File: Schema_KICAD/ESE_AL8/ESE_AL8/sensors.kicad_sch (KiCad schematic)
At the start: 22 parts, among them J201 JTAG/SWD, J202 LIDAR, J203 CB1, J204 CB3, J205 CB2, J206 CB4, J207 Moteur1, J208 Moteur2, SW201 SWITCH_CHANGEMENT, U201 ADXL343, U202 ZXBM5210-SP, U203 ZXBM5210-SP

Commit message: schema_architectural
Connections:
- net +3.3V: now also J207.5 (Pin_5), J208.5 (Pin_5)
- net +5V: no longer J207.5 (Pin_5), J208.5 (Pin_5)
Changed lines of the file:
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@@
 	)
 	(symbol
+		(lib_name "+3.3V_1")
+		(lib_id "power:+3.3V")
+		(at 115.57 167.64 90)
+		(unit 1)
+		(exclude_from_sim no)
+		(in_bom yes)
+		(on_board yes)
+		(dnp no)
+		(fields_autoplaced yes)
+		(property "Reference" "#PWR02"
+			(at 119.38 167.64 0)
+			(effects
+				(font
+					(size 1.27 1.27)
+				)
+				(hide yes)
+			)
+		)
+		(property "Value" "+3.3V"
+			(at 111.76 167.6399 90)
+			(effects
+				(font
+					(size 1.27 1.27)
+				)
+				(justify left)
+			)
+		)
+		(property "Footprint" ""
+			(at 115.57 167.64 0)
+			(effects
+				(font
+					(size 1.27 1.27)
+				)
+				(hide yes)
+			)
+		)
+		(property "Datasheet" ""
+			(at 115.57 167.64 0)
+			(effects
+				(font
+					(size 1.27 1.27)
+				)
+				(hide yes)
+			)
+		)
+		(property "Description" "Power symbol creates a global label with name \"+3.3V\""
+			(at 115.57 167.64 0)
+			(effects
+				(font
+					(size 1.27 1.27)
+				)
+				(hide yes)
+			)
+		)
+		(pin "1"
+		)
+		(instances
+			(project "ESE_AL8"
+				(path "/c3d0eb52-cd9d-4e69-bcf7-3f0716f715c6/ec07ab64-4612-44cf-8e70-ea693fb6c5ed"
+					(reference "#PWR02")
+					(unit 1)
+				)
+			)
+		)
+	)
+	(symbol
 		(lib_id "Device:C_Small")
 		(at 190.5 36.83 0)
@@
 	)
 	(symbol
-		(lib_id "power:+5V")
-		(at 115.57 167.64 90)
+		(lib_id "power:GND")
+		(at 46.99 62.23 0)
 		(unit 1)
 		(exclude_from_sim no)
@@
 		(dnp no)
 		(fields_autoplaced yes)
-		(property "Reference" "#PWR0234"
-			(at 119.38 167.64 0)
+		(property "Reference" "#PWR0211"
+			(at 46.99 68.58 0)
 			(effects
 				(font
@@
 			)
 		)
-		(property "Value" "+5V"
-			(at 111.76 167.64 90)
+		(property "Value" "GND"
+			(at 46.99 67.31 0)
 			(effects
 				(font
 					(size 1.27 1.27)
 				)
-				(justify left)
 			)
 		)
 		(property "Footprint" ""
-			(at 115.57 167.64 0)
+			(at 46.99 62.23 0)
 			(effects
 				(font
@@
 		)
 		(property "Datasheet" ""
-			(at 115.57 167.64 0)
+			(at 46.99 62.23 0)
 			(effects
 				(font
@@
 		)
 		(property "Description" ""
-			(at 115.57 167.64 0)
+			(at 46.99 62.23 0)
 			(effects
 				(font
@@
 			(project "ESE_AL8"
 				(path "/c3d0eb52-cd9d-4e69-bcf7-3f0716f715c6/ec07ab64-4612-44cf-8e70-ea693fb6c5ed"
-					(reference "#PWR0234")
+					(reference "#PWR0211")
 					(unit 1)
 				)
@@
 	)
 	(symbol
-		(lib_id "power:GND")
-		(at 46.99 62.23 0)
+		(lib_id "power:+5V")
+		(at 121.92 67.31 90)
 		(unit 1)
 		(exclude_from_sim no)
@@
 		(dnp no)
 		(fields_autoplaced yes)
-		(property "Reference" "#PWR0211"
-			(at 46.99 68.58 0)
+		(property "Reference" "#PWR0214"
+			(at 125.73 67.31 0)
 			(effects
 				(font
@@
 			)
 		)
-		(property "Value" "GND"
-			(at 46.99 67.31 0)
+		(property "Value" "+5V"
+			(at 118.11 67.31 90)
 			(effects
 				(font
 					(size 1.27 1.27)
 				)
+				(justify left)
 			)
 		)
 		(property "Footprint" ""
-			(at 46.99 62.23 0)
+			(at 121.92 67.31 0)
 			(effects
 				(font
@@
 		)
 		(property "Datasheet" ""
-			(at 46.99 62.23 0)
+			(at 121.92 67.31 0)
 			(effects
 				(font
@@
 		)
 		(property "Description" ""
-			(at 46.99 62.23 0)
+			(at 121.92 67.31 0)
 			(effects
 				(font
@@
 			(project "ESE_AL8"
 				(path "/c3d0eb52-cd9d-4e69-bcf7-3f0716f715c6/ec07ab64-4612-44cf-8e70-ea693fb6c5ed"
-					(reference "#PWR0211")
+					(reference "#PWR0214")
 					(unit 1)
 				)
@@
 	)
 	(symbol
-		(lib_id "power:+5V")
-		(at 121.92 67.31 90)
+		(lib_id "Device:R_Small")
+		(at 180.34 62.23 0)
+		(mirror y)
 		(unit 1)
 		(exclude_from_sim no)
@@
 		(on_board yes)
 		(dnp no)
-		(fields_autoplaced yes)
-		(property "Reference" "#PWR0214"
-			(at 125.73 67.31 0)
+		(property "Reference" "R202"
+			(at 185.42 60.96 0)
 			(effects
 				(font
 					(size 1.27 1.27)
 				)
-				(hide yes)
+				(justify left)
 			)
 		)
-		(property "Value" "+5V"
-			(at 118.11 67.31 90)
+		(property "Value" "2.2k"
+			(at 186.69 63.5 0)
 			(effects
 				(font
@@
 			)
 		)
-		(property "Footprint" ""
-			(at 121.92 67.31 0)
+		(property "Footprint" "Resistor_SMD:R_0603_1608Metric_Pad0.98x0.95mm_HandSolder"
+			(at 180.34 62.23 0)
 			(effects
 				(font
@@
 			)
 		)
-		(property "Datasheet" ""
-			(at 121.92 67.31 0)
+		(property "Datasheet" "~"
+			(at 180.34 62.23 0)
 			(effects
 				(font
@@
 		)
 		(property "Description" ""
-			(at 121.92 67.31 0)
+			(at 180.34 62.23 0)
 			(effects
 				(font
@@
 		(pin "1"
 		)
+		(pin "2"
+		)
 		(instances
 			(project "ESE_AL8"
 				(path "/c3d0eb52-cd9d-4e69-bcf7-3f0716f715c6/ec07ab64-4612-44cf-8e70-ea693fb6c5ed"
-					(reference "#PWR0214")
+					(reference "R202")
 					(unit 1)
 				)
@@
 	)
 	(symbol
-		(lib_id "Device:R_Small")
-		(at 180.34 62.23 0)
-		(mirror y)
+		(lib_id "power:+3.3V")
+		(at 114.3 38.1 90)
+		(mirror x)
 		(unit 1)
 		(exclude_from_sim no)
@@
 		(on_board yes)
 		(dnp no)
-		(property "Reference" "R202"
-			(at 185.42 60.96 0)
+		(fields_autoplaced yes)
+		(property "Reference" "#PWR0203"
+			(at 118.11 38.1 0)
 			(effects
 				(font
 					(size 1.27 1.27)
 				)
-				(justify left)
+				(hide yes)
 			)
 		)
-		(property "Value" "2.2k"
-			(at 186.69 63.5 0)
+		(property "Value" "+3.3V"
+			(at 110.49 38.1 90)
 			(effects
 				(font
@@
 			)
 		)
-		(property "Footprint" "Resistor_SMD:R_0603_1608Metric_Pad0.98x0.95mm_HandSolder"
-			(at 180.34 62.23 0)
+		(property "Footprint" ""
+			(at 114.3 38.1 0)
 			(effects
 				(font
@@
 			)
 		)
-		(property "Datasheet" "~"
-			(at 180.34 62.23 0)
+		(property "Datasheet" ""
+			(at 114.3 38.1 0)
 			(effects
 				(font
@@
 		)
 		(property "Description" ""
-			(at 180.34 62.23 0)
+			(at 114.3 38.1 0)
 			(effects
 				(font
@@
 		(pin "1"
 		)
-		(pin "2"
-		)
 		(instances
 			(project "ESE_AL8"
 				(path "/c3d0eb52-cd9d-4e69-bcf7-3f0716f715c6/ec07ab64-4612-44cf-8e70-ea693fb6c5ed"
-					(reference "R202")
+					(reference "#PWR0203")
 					(unit 1)
 				)
@@
 	)
 	(symbol
+		(lib_name "+3.3V_1")
 		(lib_id "power:+3.3V")
-		(at 114.3 38.1 90)
-		(mirror x)
+		(at 115.57 147.32 90)
 		(unit 1)
 		(exclude_from_sim no)
@@
 		(dnp no)
 		(fields_autoplaced yes)
-		(property "Reference" "#PWR0203"
-			(at 118.11 38.1 0)
+		(property "Reference" "#PWR01"
+			(at 119.38 147.32 0)
 			(effects
 				(font
@@
 		)
 		(property "Value" "+3.3V"
-			(at 110.49 38.1 90)
+			(at 111.76 147.3199 90)
 			(effects
 				(font
@@
 		)
 		(property "Footprint" ""
-			(at 114.3 38.1 0)
+			(at 115.57 147.32 0)
 			(effects
 				(font
@@
 		)
 		(property "Datasheet" ""
-			(at 114.3 38.1 0)
+			(at 115.57 147.32 0)
 			(effects
 				(font
@@
 			)
 		)
-		(property "Description" ""
-			(at 114.3 38.1 0)
+		(property "Description" "Power symbol creates a global label with name \"+3.3V\""
+			(at 115.57 147.32 0)
 			(effects
 				(font
@@
 		)
 		(instances
-			(project "ESE_AL8"
+			(project ""
 				(path "/c3d0eb52-cd9d-4e69-bcf7-3f0716f715c6/ec07ab64-4612-44cf-8e70-ea693fb6c5ed"
-					(reference "#PWR0203")
+					(reference "#PWR01")
 					(unit 1)
 				)
@@
 					(unit 1)
 				)
-			)
-		)
-	)
-	(symbol
-		(lib_id "power:+5V")
-		(at 115.57 147.32 90)
-		(unit 1)
-		(exclude_from_sim no)
-		(in_bom yes)
-		(on_board yes)
-		(dnp no)
-		(fields_autoplaced yes)
-		(property "Reference" "#PWR0232"
-			(at 119.38 147.32 0)
-			(effects
-				(font
-					(size 1.27 1.27)
-				)
-				(hide yes)
-			)
-		)
-		(property "Value" "+5V"
-			(at 111.76 147.32 90)
-			(effects
-				(font
-					(size 1.27 1.27)
-				)
-				(justify left)
-			)
-		)
-		(property "Footprint" ""
-			(at 115.57 147.32 0)
-			(effects
-				(font
-					(size 1.27 1.27)
-				)
-				(hide yes)
-			)
-		)
-		(property "Datasheet" ""
-			(at 115.57 147.32 0)
-			(effects
-				(font
-					(size 1.27 1.27)
-				)
-				(hide yes)
-			)
-		)
-		(property "Description" ""
-			(at 115.57 147.32 0)
-			(effects
-				(font
-					(size 1.27 1.27)
-				)
-				(hide yes)
-			)
-		)
-		(pin "1"
-		)
-		(instances
-			(project "ESE_AL8"
-				(path "/c3d0eb52-cd9d-4e69-bcf7-3f0716f715c6/ec07ab64-4612-44cf-8e70-ea693fb6c5ed"
-					(reference "#PWR0232")
-					(unit 1)
-				)

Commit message: commit pour 18/09
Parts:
- added C203: 10u, Capacitor_SMD:C_0603_1608Metric_Pad1.08x0.95mm_HandSolder, symbol Device:C_Small
- added JP201: TestRX, symbol Jumper:SolderJumper_2_Open
- added JP202: TestTX, symbol Jumper:SolderJumper_2_Open
- added JP203: TestSDA, symbol Jumper:SolderJumper_2_Open
- renumbered C206 to C201, C203 to C202, C208 to C204, C207 to C205, C205 to C206, C204 to C207, C201 to C208, C202 to C209, J207 to J202, J208 to J203, J202 to J204, J203 to J205, J205 to J206, J204 to J207, J206 to J208, U203 to U201, U201 to U203
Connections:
- net GND: now also C203.1
- net VIN: now also C203.2
- net CHMT renamed CHAT/SOURIS
- net DEV_EN renamed DEV_EN_LIDAR
- net INT1 renamed INT1_ACCELERO
- net INT2: no longer names the net of U203.9 (INT2)
- net M_EN renamed M_EN_LIDAR
- net M_SCTR renamed M_SCTR_LIDAR
- net RX renamed RX_LIDAR
- net RX2: no longer names the net of J201.13 (Pin_13)
- net RX2: now also JP201.2 (B)
- net SCL renamed SCL_ACCELERO
- net SDA: no longer names the net of R202.1, U203.13 (SDA/SDI/SDIO)
- net SDA: now also JP203.2 (B)
- net TX renamed TX_LIDAR
- net TX2: no longer names the net of J201.14 (Pin_14)
- net TX2: now also JP202.1 (A)
- new net RX2_JTAG: JP201.1 (A)
- new net SDA_ACCELERO: JP203.1 (A)
- new net TX2_JTAG: JP202.2 (B)
- no-connect marks 6 -> 7
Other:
- note added: "Capteur de bordure(CB)"
- note removed: "Capteur de bordure"
- moved on the sheet: R201, R202

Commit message: LE 25 /09/2024 10:31
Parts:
- removed JP203: TestSDA, symbol Jumper:SolderJumper_2_Open
- removed SW201: SWITCH_CHANGEMENT, Button_Switch_THT:SW_Slide-03_Wuerth-WS-SLTV_10x2.5x6.4_P2.54mm, symbol Switch:SW_SPDT
- added C203: 10u, Capacitor_SMD:C_0603_1608Metric_Pad1.08x0.95mm_HandSolder, symbol Device:C_Small
- added SW201: SW_c/s, Button_Switch_SMD:SW_Push_1P1T_NO_6x6mm_H9.5mm, symbol Switch:SW_Push
- added TP201: TestPoint, TestPoint:TestPoint_Pad_D1.0mm, symbol Connector:TestPoint
- C201, C202: value 100n -> 1u; footprint Capacitor_SMD:C_0603_1608Metric_Pad1.08x0.95mm_HandSolder -> Capacitor_SMD:C_0402_1005Metric_Pad0.74x0.62mm_HandSolder
- C205: renamed from C204; footprint Capacitor_SMD:C_0603_1608Metric_Pad1.08x0.95mm_HandSolder -> Capacitor_SMD:C_0402_1005Metric_Pad0.74x0.62mm_HandSolder
- C206: renamed from C205; footprint Capacitor_SMD:C_0603_1608Metric_Pad1.08x0.95mm_HandSolder -> Capacitor_SMD:C_0402_1005Metric_Pad0.74x0.62mm_HandSolder
- C207: renamed from C206; footprint Capacitor_SMD:C_0603_1608Metric_Pad1.08x0.95mm_HandSolder -> Capacitor_SMD:C_0402_1005Metric_Pad0.74x0.62mm_HandSolder
- C208: renamed from C207; footprint Capacitor_SMD:C_0603_1608Metric_Pad1.08x0.95mm_HandSolder -> Capacitor_SMD:C_0402_1005Metric_Pad0.74x0.62mm_HandSolder
- C209: renamed from C208; footprint Capacitor_SMD:C_0603_1608Metric_Pad1.08x0.95mm_HandSolder -> Capacitor_SMD:C_0402_1005Metric_Pad0.74x0.62mm_HandSolder
- C210: renamed from C209; footprint Capacitor_SMD:C_0603_1608Metric_Pad1.08x0.95mm_HandSolder -> Capacitor_SMD:C_0402_1005Metric_Pad0.74x0.62mm_HandSolder
- JP201, JP202: footprint (none) -> Jumper:SolderJumper-2_P1.3mm_Open_TrianglePad1.0x1.5mm
- R201, R202: footprint Resistor_SMD:R_0603_1608Metric_Pad0.98x0.95mm_HandSolder -> Resistor_SMD:R_0402_1005Metric_Pad0.72x0.64mm_HandSolder
- renumbered C203 to C204
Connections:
- net CB_IN2 is gone; now on net CB_IN: J206.4 (Pin_4)
- net CB_IN3 is gone; now on net CB_IN: J207.4 (Pin_4)
- net CB_IN4 is gone; now on net CB_IN: J208.4 (Pin_4)
- net RX2_JTAG is gone; now on an unnamed net: JP201.1 (A)
- net CHAT/SOURIS: now also SW201.1
- net GND: now also C203.1, SW201.2
- net SDA_ACCELERO: now also R202.1, U203.13 (SDA/SDI/SDIO), TP201.1
- net VIN: now also C203.2
- net at J201.13 (Pin_13): no longer JP201.2 (B)
- net CB_IN1 renamed CB_IN
- net TX2_JTAG renamed TX_SWD
- new net RX_SWD: JP201.2 (B)

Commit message: commit du code et kicad modifié
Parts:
- removed C201, C202: 1u, Capacitor_SMD:C_0402_1005Metric_Pad0.74x0.62mm_HandSolder, symbol Device:C_Small
- removed C203, C204: 10u, Capacitor_SMD:C_0603_1608Metric_Pad1.08x0.95mm_HandSolder, symbol Device:C_Small
- removed C205, C206, C207, C208: 100n, Capacitor_SMD:C_0402_1005Metric_Pad0.74x0.62mm_HandSolder, symbol Device:C_Small
- removed J201: JTAG/SWD, Connector_PinHeader_1.27mm:PinHeader_2x07_P1.27mm_Vertical_SMD, symbol Connector_Generic:Conn_02x07_Odd_Even
- removed J204: LIDAR, Connector_JST:JST_EH_B7B-EH-A_1x07_P2.50mm_Vertical, symbol Connector_Generic:Conn_01x07
- removed JP201: TestRX, Jumper:SolderJumper-2_P1.3mm_Open_TrianglePad1.0x1.5mm, symbol Jumper:SolderJumper_2_Open
- removed JP202: TestTX, Jumper:SolderJumper-2_P1.3mm_Open_TrianglePad1.0x1.5mm, symbol Jumper:SolderJumper_2_Open
- removed U201, U202: ZXBM5210-SP, Package_SO:Diodes_SO-8EP, symbol Driver_Motor:ZXBM5210-SP
- added J3: LIDAR, symbol Connector:Screw_Terminal_01x08
- added TP1, TP2: TestPoint, TestPoint:TestPoint_Pad_D1.0mm, symbol Connector:TestPoint
- C210: value 1u -> 100n
- R201, R202: value 2.2k -> 1k
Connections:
- net +5V: now also J3.1 (Pin_1)
- net DEV_EN_LIDAR: now also J3.6 (Pin_6)
- net GND: now also J3.4 (Pin_4)
- net INT1_ACCELERO: now also TP2.1
- net M_EN_LIDAR: now also J3.5 (Pin_5)
- net M_SCTR_LIDAR: now also J3.7 (Pin_7)
- net RX_LIDAR: now also J3.3 (Pin_3)
- net TX_LIDAR: now also J3.2 (Pin_2)
- net SCL_ACCELERO renamed SCL
- net SCL: now also TP1.1
- net SDA_ACCELERO renamed SDA
- no-connect marks 7 -> 4
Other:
- note removed: "Drivers"
- note removed: "STDC14"
- moved on the sheet: C209, C210, J202, J203, J205, J206, J207, J208, R201, R202, SW201, TP201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

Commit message: commit pour le schema
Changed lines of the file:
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@@
+		)
+	)
+	(wire
+		(pts
+			(xy 162.56 132.08) (xy 168.91 132.08)
+		)
+		(stroke
+			(width 0)
+			(type default)
 		)
 	)
@@
 		)
 	)
+	(hierarchical_label "5v"
+		(shape input)
+		(at 165.1 132.08 90)
+		(fields_autoplaced yes)
+		(effects
+			(font
+				(size 1.27 1.27)
+			)
+			(justify left)
+		)
+	)
 	(hierarchical_label "M_EN_LIDAR"
 		(shape input)
@@
 	(symbol
 		(lib_id "power:+5V")
-		(at 168.91 132.08 90)
+		(at 162.56 132.08 90)
 		(unit 1)
 		(exclude_from_sim no)
@@
 		(fields_autoplaced yes)
 		(property "Reference" "#PWR0219"
-			(at 172.72 132.08 0)
+			(at 166.37 132.08 0)
 			(effects
 				(font
@@
 		)
 		(property "Value" "+5V"
-			(at 165.1 132.08 90)
+			(at 158.75 132.08 90)
 			(effects
 				(font
@@
 		)
 		(property "Footprint" ""
-			(at 168.91 132.08 0)
+			(at 162.56 132.08 0)
 			(effects
 				(font
@@
 		)
 		(property "Datasheet" ""
-			(at 168.91 132.08 0)
+			(at 162.56 132.08 0)
 			(effects
 				(font
@@
 		)
 		(property "Description" ""
-			(at 168.91 132.08 0)
-			(effects
-				(font
+			(at 162.56 132.08 0)
+			(effects
+				(font

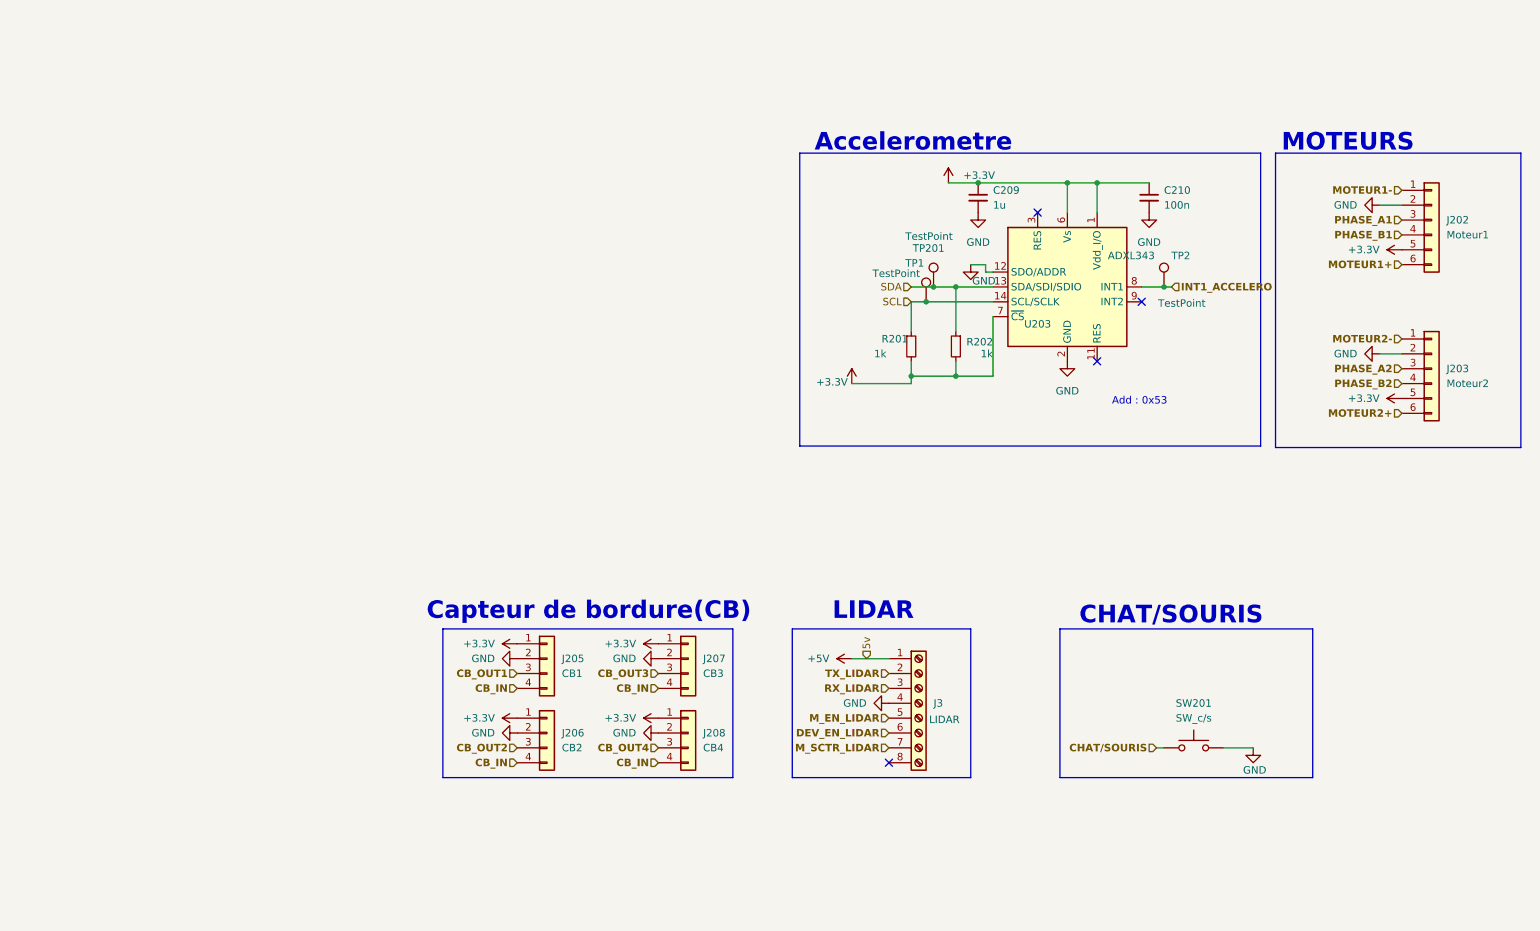
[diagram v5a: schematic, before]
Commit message: Routage aprés correction
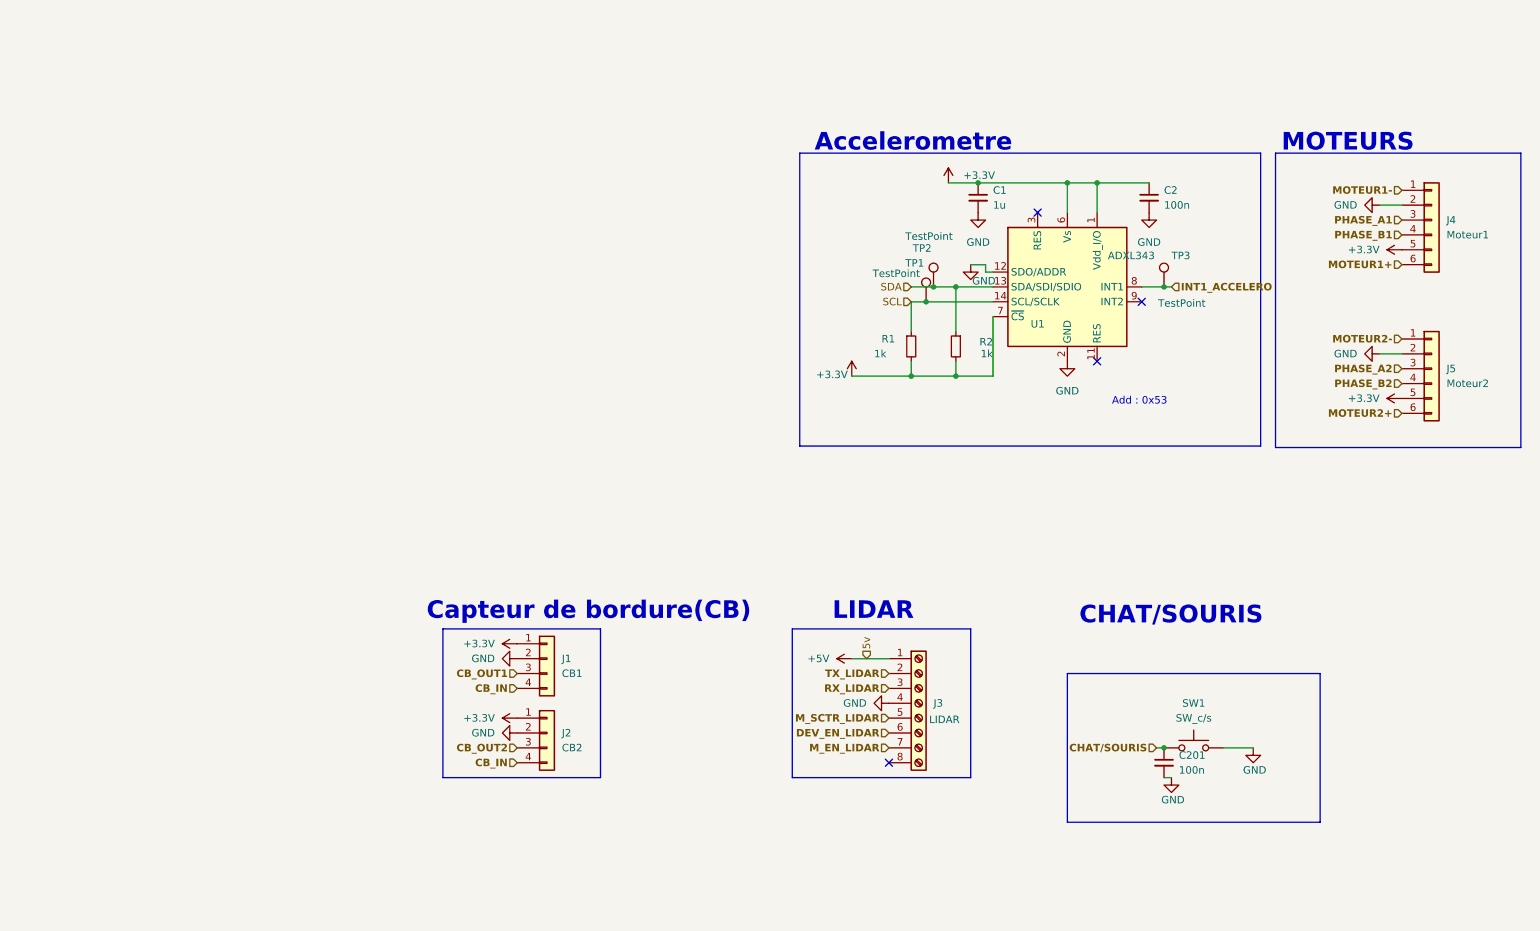
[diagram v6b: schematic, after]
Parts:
- removed J207: CB3, Connector_JST:JST_EH_B4B-EH-A_1x04_P2.50mm_Vertical, symbol Connector_Generic:Conn_01x04
- removed J208: CB4, Connector_JST:JST_EH_B4B-EH-A_1x04_P2.50mm_Vertical, symbol Connector_Generic:Conn_01x04
- added C201: 100n, Capacitor_SMD:C_0402_1005Metric, symbol Device:C_Small
- C1: renamed from C209; footprint Capacitor_SMD:C_0402_1005Metric_Pad0.74x0.62mm_HandSolder -> Capacitor_SMD:C_0603_1608Metric
- C2: renamed from C210; footprint Capacitor_SMD:C_0402_1005Metric_Pad0.74x0.62mm_HandSolder -> Capacitor_SMD:C_0402_1005Metric
- J1: renamed from J205; footprint Connector_JST:JST_EH_B4B-EH-A_1x04_P2.50mm_Vertical -> Connector_JST:JST_XH_S4B-XH-A_1x04_P2.50mm_Horizontal
- J2: renamed from J206; footprint Connector_JST:JST_EH_B4B-EH-A_1x04_P2.50mm_Vertical -> Connector_JST:JST_XH_S4B-XH-A_1x04_P2.50mm_Horizontal
- J3: footprint (none) -> Connector_JST:JST_XH_S8B-XH-A_1x08_P2.50mm_Horizontal
- J4: renamed from J202; footprint Connector_JST:JST_EH_B6B-EH-A_1x06_P2.50mm_Vertical -> Connector_JST:JST_XH_S6B-XH-A_1x06_P2.50mm_Horizontal
- J5: renamed from J203; footprint Connector_JST:JST_EH_B6B-EH-A_1x06_P2.50mm_Vertical -> Connector_JST:JST_XH_S6B-XH-A_1x06_P2.50mm_Horizontal
- R1: renamed from R201; footprint Resistor_SMD:R_0402_1005Metric_Pad0.72x0.64mm_HandSolder -> Resistor_SMD:R_0402_1005Metric
- R2: renamed from R202; footprint Resistor_SMD:R_0402_1005Metric_Pad0.72x0.64mm_HandSolder -> Resistor_SMD:R_0402_1005Metric
- SW1: renamed from SW201; footprint Button_Switch_SMD:SW_Push_1P1T_NO_6x6mm_H9.5mm -> STM32:SW_Push_1P1T_NO_6x6mm_H9.5mm
- renumbered TP201 to TP2, TP2 to TP3, U203 to U1
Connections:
- net CHAT/SOURIS: now also C201.1
- net GND: now also C201.2
- net M_EN_LIDAR: now also J3.7 (Pin_7); no longer J3.5 (Pin_5)
- net M_SCTR_LIDAR: now also J3.5 (Pin_5); no longer J3.7 (Pin_7)

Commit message: Commit midif pcb 2020
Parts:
- added R16, R17: 1k, Resistor_SMD:R_0402_1005Metric, symbol Device:R_Small
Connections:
- net +3.3V: now also R17.1
- net CHAT/SOURIS: now also R16.1; no longer SW1.1
- new net: R16.2, R17.2, SW1.1
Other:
- moved on the sheet: C201, SW1
